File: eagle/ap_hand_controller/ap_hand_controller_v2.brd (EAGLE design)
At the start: 55.9 x 152.4 mm, 27 parts, among them IC1 MAX3232CSE, J1 RJ11(To AP), J2 To AP, SW1 BACK, SW2 MENU, SW3 reset, U1 SPARKFUN_PRO_MICRO, U2 R78E3.3-0.5

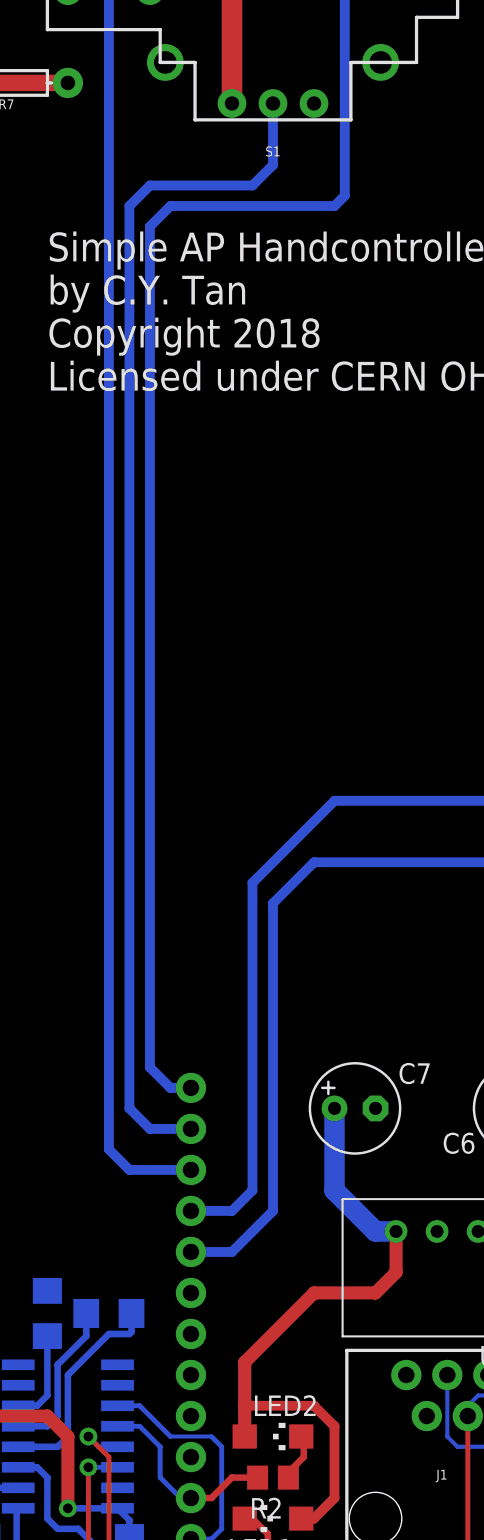
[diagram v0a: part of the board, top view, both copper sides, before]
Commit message: Fixed Vcc unconnected bug in ap_hand_controller_v2.brd. Thanks to Andrew (ab15Kath) for discovering this bug.
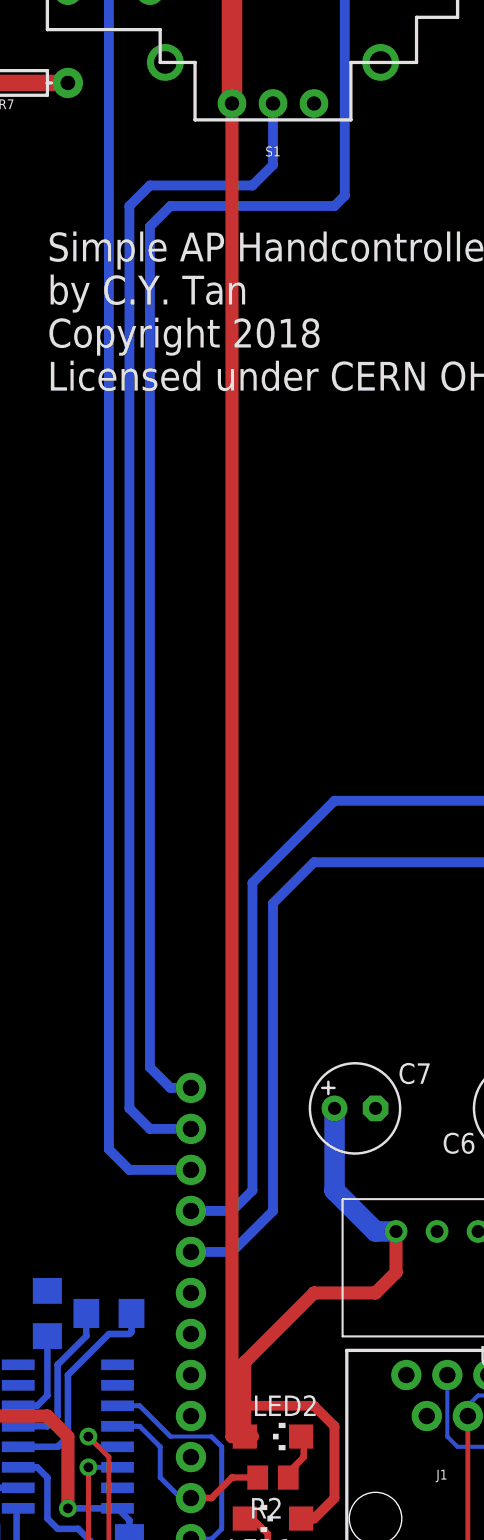
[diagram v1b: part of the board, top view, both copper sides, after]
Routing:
- net VCC: track 282.8 -> 366.6 mm
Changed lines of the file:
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@@
 <wire x1="44.45" y1="101.6" x2="44.45" y2="104.14" width="1.016" layer="1"/>
 <wire x1="44.45" y1="104.14" x2="46.99" y2="106.68" width="1.016" layer="1"/>
-<wire x1="19.05" y1="4.9784" x2="26.19" y2="10.16" width="0" layer="19" extent="1-16"/>
+<wire x1="26.67" y1="10.16" x2="25.4" y2="10.16" width="0.8128" layer="1"/>
+<wire x1="25.4" y1="10.16" x2="25.4" y2="92.71" width="0.8128" layer="1"/>
+<wire x1="26.67" y1="10.16" x2="26.19" y2="10.16" width="0" layer="19" extent="1-1"/>
 </signal>
 <signal name="N$1">
